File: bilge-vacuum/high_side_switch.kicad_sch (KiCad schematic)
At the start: 5 parts, among them U9 TPS27S100A

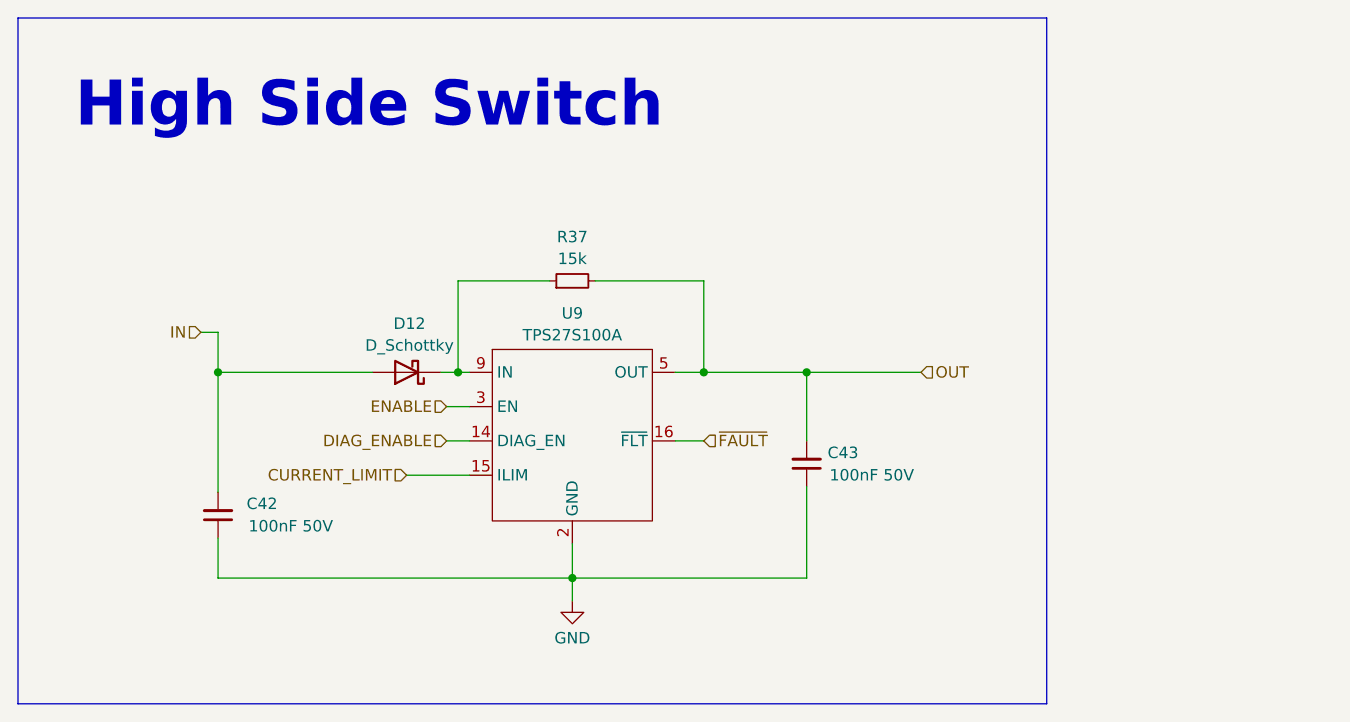
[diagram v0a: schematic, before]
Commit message: Assign the bulk of parts, some passives still need custom footprints.
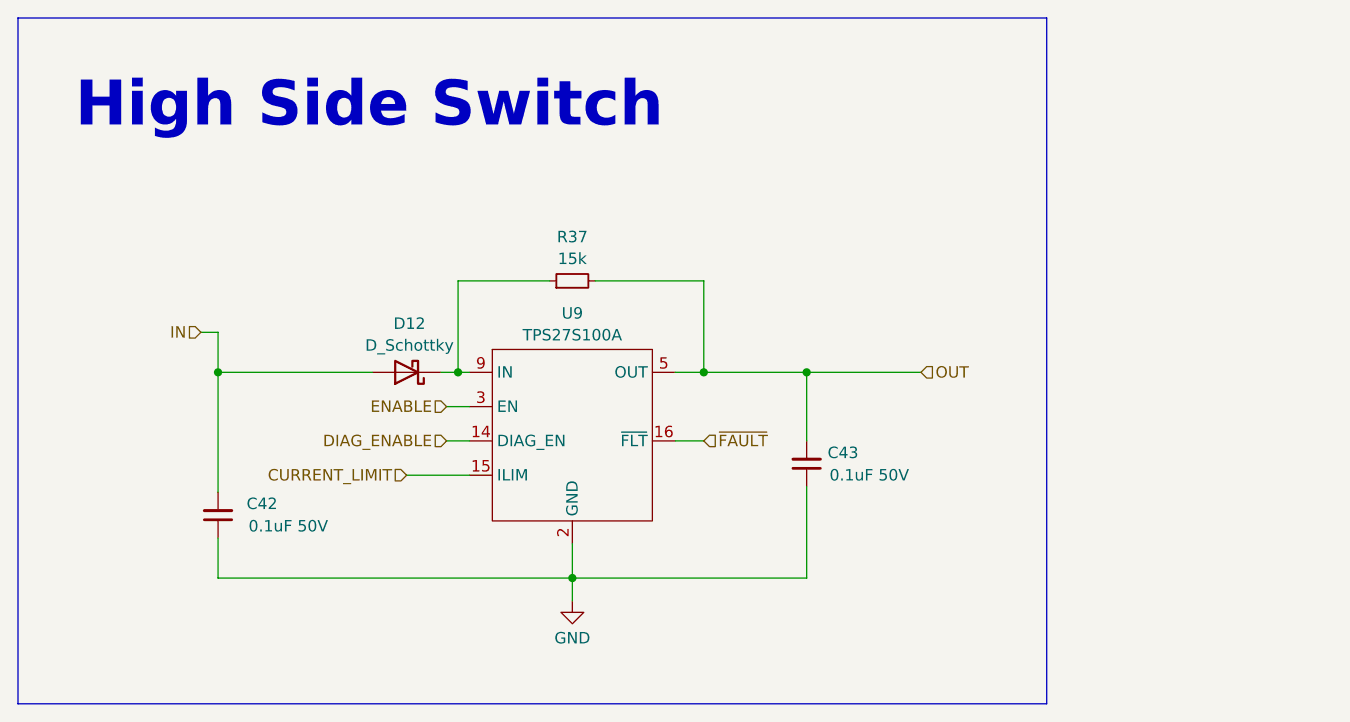
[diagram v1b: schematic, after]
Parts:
- C42, C43: value 100nF 50V -> 0.1uF 50V; footprint (none) -> Capacitor_SMD:C_0805_2012Metric
- D12: footprint (none) -> Custom Parts:SMA
- R37: footprint (none) -> Resistor_SMD:R_0805_2012Metric
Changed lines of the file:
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@@
       (effects (font (size 1.27 1.27)))
     )
-    (property "Footprint" "" (at 62.23 58.42 0)
+    (property "Footprint" "Custom Parts:SMA" (at 62.23 58.42 0)
       (effects (font (size 1.27 1.27)) hide)
     )
@@
       (effects (font (size 1.27 1.27)) (justify right))
     )
-    (property "Value" "100nF 50V" (at 44.6659 75.5135 0)
-      (effects (font (size 1.27 1.27)) (justify right))
-    )
-    (property "Footprint" "" (at 41.275 74.295 0)
+    (property "Value" "0.1uF 50V" (at 44.6659 75.5135 0)
+      (effects (font (size 1.27 1.27)) (justify right))
+    )
+    (property "Footprint" "Capacitor_SMD:C_0805_2012Metric" (at 41.275 74.295 0)
       (effects (font (size 1.27 1.27)) hide)
     )
@@
       (effects (font (size 1.27 1.27)))
     )
-    (property "Footprint" "" (at 80.645 48.26 0)
+    (property "Footprint" "Resistor_SMD:R_0805_2012Metric" (at 80.645 48.26 0)
       (effects (font (size 1.27 1.27)) hide)
     )
@@
       (effects (font (size 1.27 1.27)) (justify right))
     )
-    (property "Value" "100nF 50V" (at 109.22 69.85 0)
-      (effects (font (size 1.27 1.27)) (justify right))
-    )
-    (property "Footprint" "" (at 106.68 68.58 0)
-      (effects (font (size 1.27 1.27)) hide)
-    )
+    (property "Value" "0.1uF 50V" (at 109.22 69.85 0)
+      (effects (font (size 1.27 1.27)) (justify right))
+    )
+    (property "Footprint" "Capacitor_SMD:C_0805_2012Metric" (at 106.68 68.58 0)
+      (effects (font (size 1.27 1.27)) hide)
+    )

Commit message: bilge vac 1v0
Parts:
- added D7: GREEN, LED_SMD:LED_0805_2012Metric, symbol Device:LED
- added R26: 2.2k, Resistor_SMD:R_0805_2012Metric, symbol Device:R
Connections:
- net GND: now also R26.2
- net OUT: now also D7.2 (A)
- new net: D7.1 (K), R26.1
- now unconnected: U9.13 (NC), U9.4 (NC)
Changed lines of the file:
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@@
   (junction (at 67.945 58.42) (diameter 0) (color 0 0 0 0)
   )
+  (junction (at 120.65 58.42) (diameter 0) (color 0 0 0 0)
+  )
   (junction (at 106.68 58.42) (diameter 0) (color 0 0 0 0)
   )
@@
     (stroke (width 0) (type default))
   )
+  (wire (pts (xy 120.65 67.31) (xy 120.65 70.485))
+    (stroke (width 0) (type default))
+  )
   (wire (pts (xy 41.275 58.42) (xy 41.275 71.755))
     (stroke (width 0) (type default))
@@
     (stroke (width 0) (type default))
   )
+  (wire (pts (xy 120.65 78.105) (xy 120.65 81.915))
+    (stroke (width 0) (type default))
+  )
   (wire (pts (xy 80.645 81.28) (xy 80.645 83.82))
     (stroke (width 0) (type default))
@@
     (stroke (width 0) (type default))
   )
-  (wire (pts (xy 106.68 58.42) (xy 119.38 58.42))
+  (wire (pts (xy 106.68 58.42) (xy 120.65 58.42))
     (stroke (width 0) (type default))
   )
@@
     (stroke (width 0) (type default))
   )
+  (wire (pts (xy 120.65 58.42) (xy 127.635 58.42))
+    (stroke (width 0) (type default))
+  )
   (wire (pts (xy 62.23 69.85) (xy 69.215 69.85))
     (stroke (width 0) (type default))
@@
     (stroke (width 0) (type default))
   )
-  (rectangle (start 19.05 19.05) (end 133.35 95.25)
+  (wire (pts (xy 120.65 58.42) (xy 120.65 59.69))
+    (stroke (width 0) (type default))
+  )
+  (rectangle (start 19.05 19.05) (end 139.7 95.25)
     (stroke (width 0) (type default))
     (fill (type none))
@@
     (effects (font (size 5 5) bold) (justify left bottom))
   )
-  (hierarchical_label "OUT" (shape input) (at 119.38 58.42 0) (fields_autoplaced)
+  (hierarchical_label "OUT" (shape input) (at 127.635 58.42 0) (fields_autoplaced)
     (effects (font (size 1.27 1.27)) (justify left))
   )
@@
   (hierarchical_label "CURRENT_LIMIT" (shape input) (at 62.23 69.85 180) (fields_autoplaced)
     (effects (font (size 1.27 1.27)) (justify right))
+  )
+  (symbol (lib_id "Device:R") (at 120.65 74.295 0) (unit 1)
+    (in_bom yes) (on_board yes) (dnp no) (fields_autoplaced)
+    (property "Reference" "R26" (at 122.428 73.0829 0)
+      (effects (font (size 1.27 1.27)) (justify left))
+    )
+    (property "Value" "2.2k" (at 122.428 75.5071 0)
+      (effects (font (size 1.27 1.27)) (justify left))
+    )
+    (property "Footprint" "Resistor_SMD:R_0805_2012Metric" (at 118.872 74.295 90)
+      (effects (font (size 1.27 1.27)) hide)
+    )
+    (property "Datasheet" "~" (at 120.65 74.295 0)
+      (effects (font (size 1.27 1.27)) hide)
+    )
+    (pin "1")
+    (pin "2")
+    (instances
+      (project "bilge-vacuum"
+        (path "/08405ba3-6912-4dc1-869a-b11176a5bc8a"
+          (reference "R26") (unit 1)
+        )
+        (path "/08405ba3-6912-4dc1-869a-b11176a5bc8a/8a95e837-e0e7-4b78-93e7-7ab95e7c82dc"
+          (reference "R27") (unit 1)
+        )
+        (path "/08405ba3-6912-4dc1-869a-b11176a5bc8a/16850e27-1e2e-4e85-af36-1238f6162217/75bab21f-91ff-472d-9eda-e6cf042b5388"
+          (reference "R48") (unit 1)
+        )
+        (path "/08405ba3-6912-4dc1-869a-b11176a5bc8a/16850e27-1e2e-4e85-af36-1238f6162217/c0c27d52-e195-48ac-b3ac-e8956acbf957"
+          (reference "R58") (unit 1)
+        )
+        (path "/08405ba3-6912-4dc1-869a-b11176a5bc8a/16850e27-1e2e-4e85-af36-1238f6162217/b242a460-8d51-4ac5-8702-0964ca4c595f"
+          (reference "R59") (unit 1)
+        )
+        (path "/08405ba3-6912-4dc1-869a-b11176a5bc8a/16850e27-1e2e-4e85-af36-1238f6162217/4c1623b3-0ea5-4447-9ca6-cb881a6787c5"
+          (reference "R60") (unit 1)
+        )
+        (path "/08405ba3-6912-4dc1-869a-b11176a5bc8a/16850e27-1e2e-4e85-af36-1238f6162217/d3a4e861-8bd1-49e1-a580-0fd3f4c593c9"
+          (reference "R61") (unit 1)
+        )
+      )
+    )
   )
   (symbol (lib_id "Device:D_Schottky") (at 62.23 58.42 180) (unit 1)
@@
     )
   )
+  (symbol (lib_id "power:GND") (at 120.65 81.915 0) (unit 1)
+    (in_bom yes) (on_board yes) (dnp no) (fields_autoplaced)
+    (property "Reference" "#PWR022" (at 120.65 88.265 0)
+      (effects (font (size 1.27 1.27)) hide)
+    )
+    (property "Value" "GND" (at 120.65 86.0481 0)
+      (effects (font (size 1.27 1.27)))
+    )
+    (property "Footprint" "" (at 120.65 81.915 0)
+      (effects (font (size 1.27 1.27)) hide)
+    )
+    (property "Datasheet" "" (at 120.65 81.915 0)
+      (effects (font (size 1.27 1.27)) hide)
+    )
+    (pin "1")
+    (instances
+      (project "bilge-vacuum"
+        (path "/08405ba3-6912-4dc1-869a-b11176a5bc8a"
+          (reference "#PWR022") (unit 1)
+        )
+        (path "/08405ba3-6912-4dc1-869a-b11176a5bc8a/8a95e837-e0e7-4b78-93e7-7ab95e7c82dc"
+          (reference "#PWR029") (unit 1)
+        )
+        (path "/08405ba3-6912-4dc1-869a-b11176a5bc8a/16850e27-1e2e-4e85-af36-1238f6162217/75bab21f-91ff-472d-9eda-e6cf042b5388"
+          (reference "#PWR015") (unit 1)
+        )
+        (path "/08405ba3-6912-4dc1-869a-b11176a5bc8a/16850e27-1e2e-4e85-af36-1238f6162217/c0c27d52-e195-48ac-b3ac-e8956acbf957"
+          (reference "#PWR060") (unit 1)
+        )
+        (path "/08405ba3-6912-4dc1-869a-b11176a5bc8a/16850e27-1e2e-4e85-af36-1238f6162217/b242a460-8d51-4ac5-8702-0964ca4c595f"
+          (reference "#PWR061") (unit 1)
+        )
+        (path "/08405ba3-6912-4dc1-869a-b11176a5bc8a/16850e27-1e2e-4e85-af36-1238f6162217/4c1623b3-0ea5-4447-9ca6-cb881a6787c5"
+          (reference "#PWR062") (unit 1)
+        )
+        (path "/08405ba3-6912-4dc1-869a-b11176a5bc8a/16850e27-1e2e-4e85-af36-1238f6162217/d3a4e861-8bd1-49e1-a580-0fd3f4c593c9"
+          (reference "#PWR063") (unit 1)
+        )
+      )
+    )
+  )
+  (symbol (lib_id "Device:LED") (at 120.65 63.5 90) (unit 1)
+    (in_bom yes) (on_board yes) (dnp no) (fields_autoplaced)
+    (property "Reference" "D7" (at 124.46 63.8175 90)
+      (effects (font (size 1.27 1.27)) (justify right))
+    )
+    (property "Value" "GREEN" (at 124.46 66.3575 90)
+      (effects (font (size 1.27 1.27)) (justify right))
+    )
+    (property "Footprint" "LED_SMD:LED_0805_2012Metric" (at 120.65 63.5 0)
+      (effects (font (size 1.27 1.27)) hide)
+    )
+    (property "Datasheet" "~" (at 120.65 63.5 0)
+      (effects (font (size 1.27 1.27)) hide)
+    )
+    (pin "1")
+    (pin "2")
+    (instances
+      (project "bilge-vacuum"
+        (path "/08405ba3-6912-4dc1-869a-b11176a5bc8a"
+          (reference "D7") (unit 1)
+        )
+        (path "/08405ba3-6912-4dc1-869a-b11176a5bc8a/8a95e837-e0e7-4b78-93e7-7ab95e7c82dc"
+          (reference "D7") (unit 1)
+        )
+        (path "/08405ba3-6912-4dc1-869a-b11176a5bc8a/16850e27-1e2e-4e85-af36-1238f6162217/75bab21f-91ff-472d-9eda-e6cf042b5388"
+          (reference "D14") (unit 1)
+        )
+        (path "/08405ba3-6912-4dc1-869a-b11176a5bc8a/16850e27-1e2e-4e85-af36-1238f6162217/c0c27d52-e195-48ac-b3ac-e8956acbf957"
+          (reference "D15") (unit 1)
+        )
+        (path "/08405ba3-6912-4dc1-869a-b11176a5bc8a/16850e27-1e2e-4e85-af36-1238f6162217/b242a460-8d51-4ac5-8702-0964ca4c595f"
+          (reference "D16") (unit 1)
+        )
+        (path "/08405ba3-6912-4dc1-869a-b11176a5bc8a/16850e27-1e2e-4e85-af36-1238f6162217/4c1623b3-0ea5-4447-9ca6-cb881a6787c5"
+          (reference "D17") (unit 1)
+        )
+        (path "/08405ba3-6912-4dc1-869a-b11176a5bc8a/16850e27-1e2e-4e85-af36-1238f6162217/d3a4e861-8bd1-49e1-a580-0fd3f4c593c9"
+          (reference "D18") (unit 1)
+        )
+      )
+    )
+  )
   (symbol (lib_id "Custom Parts:TPS27S100A") (at 80.645 64.77 0) (unit 1)
     (in_bom yes) (on_board yes) (dnp no) (fields_autoplaced)
@@
       (effects (font (size 1.27 1.27)) hide)
     )
+    (pin "1")
     (pin "10")
     (pin "11")
@@
     (pin "8")
     (pin "9")
-    (pin "NC")
-    (instances
-      (project "bilge-vacuum"
+    (instances
+      (project "bilge-vacuum"

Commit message: Fixes
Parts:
- added R62, R67, R72: 10k 1%, Resistor_SMD:R_0805_2012Metric, symbol Device:R_Small
- D12: value D_Schottky -> B260AQ-13-F
- R26: value 2.2k -> 10k 1%
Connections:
- net DIAG_ENABLE: now also R62.1
- net ENABLE: now also R67.1
- net GND: now also R62.2, R67.2
- net ~{FAULT}: now also R72.1
- new net IO_VDD: R72.2
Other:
- moved on the sheet: C42, C43, D12, D7, R26, R37, U9
